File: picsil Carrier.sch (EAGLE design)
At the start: 43 parts, among them IC1 NAND, J1 STX-3120-3BM, J2 STX-3120-3BM, J3 STX-3120-3BM, J5 S2B-PH-SM4-TB(LF)(SN), J6 47346-1001, Q1 MMBT2222A, U1 MB85RC256VPF-G-JNERE2, U11 BORON, U2 TPL5010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

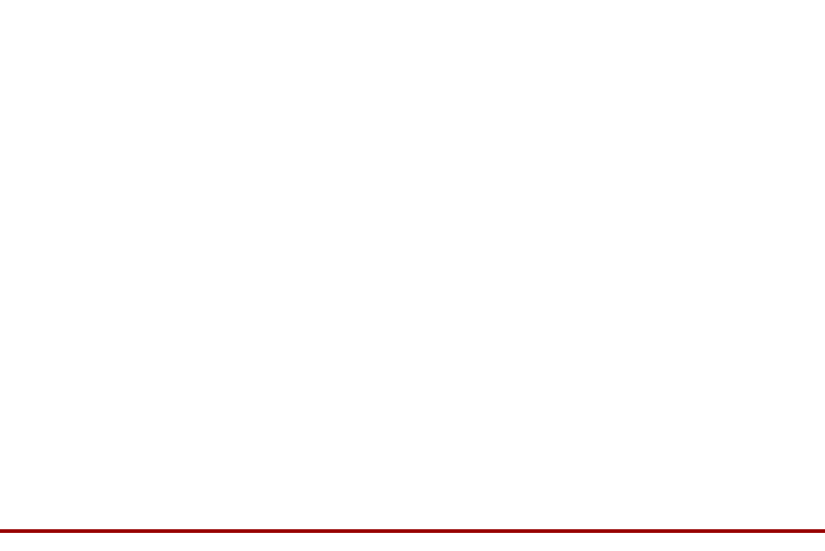
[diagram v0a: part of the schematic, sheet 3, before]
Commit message: mounting holes and fiducials
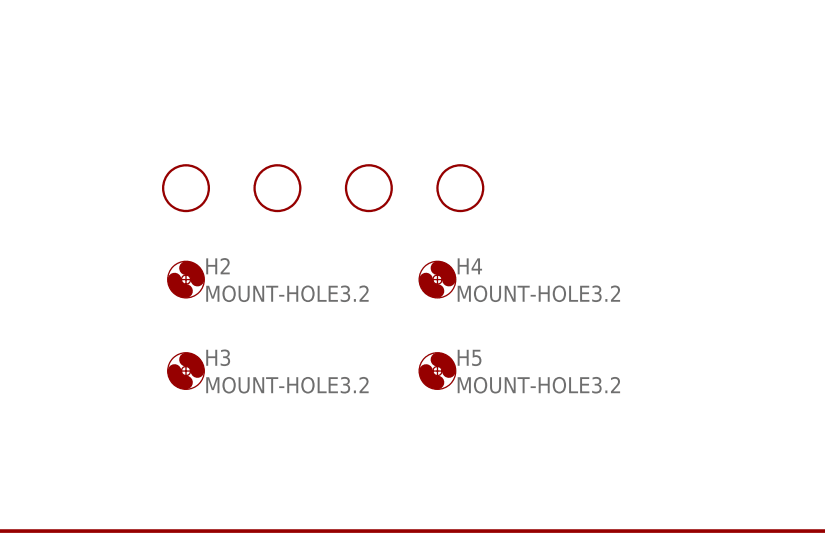
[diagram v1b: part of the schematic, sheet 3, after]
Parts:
- added H2, H3, H4, H5: MOUNT-HOLE3.2, holes:MOUNT-HOLE3.2
- added U$1, U$2, U$3, U$4: FIDUCIAL, adafruit:FIDUCIAL
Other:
- note added: "Fiducials and Holes"
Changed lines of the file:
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@@
 <setting verticaltext="up"/>
 </settings>
-<grid distance="0.1" unitdist="inch" unit="inch" style="lines" multiple="1" display="no" altdistance="0.01" altunitdist="inch" altunit="inch"/>
+<grid distance="0.1" unitdist="inch" unit="inch" style="lines" multiple="1" display="yes" altdistance="0.01" altunitdist="inch" altunit="inch"/>
 <layers>
 <layer number="1" name="Top" color="4" fill="1" visible="no" active="no"/>
@@
 <part name="J6" library="SamacSys_Parts" deviceset="47346-1001" device=""/>
 <part name="D4" library="SamacSys_Parts" deviceset="BYS12-90-M3_TR" device=""/>
+<part name="U$1" library="adafruit" library_urn="urn:adsk.eagle:library:420" deviceset="FIDUCIAL" device="" package3d_urn="urn:adsk.eagle:package:6240632/1"/>
+<part name="U$2" library="adafruit" library_urn="urn:adsk.eagle:library:420" deviceset="FIDUCIAL" device="" package3d_urn="urn:adsk.eagle:package:6240632/1"/>
+<part name="U$3" library="adafruit" library_urn="urn:adsk.eagle:library:420" deviceset="FIDUCIAL" device="" package3d_urn="urn:adsk.eagle:package:6240632/1"/>
+<part name="U$4" library="adafruit" library_urn="urn:adsk.eagle:library:420" deviceset="FIDUCIAL" device="" package3d_urn="urn:adsk.eagle:package:6240632/1"/>
+<part name="H2" library="holes" library_urn="urn:adsk.eagle:library:237" deviceset="MOUNT-HOLE" device="3.2" package3d_urn="urn:adsk.eagle:package:14275/1"/>
+<part name="H3" library="holes" library_urn="urn:adsk.eagle:library:237" deviceset="MOUNT-HOLE" device="3.2" package3d_urn="urn:adsk.eagle:package:14275/1"/>
+<part name="H4" library="holes" library_urn="urn:adsk.eagle:library:237" deviceset="MOUNT-HOLE" device="3.2" package3d_urn="urn:adsk.eagle:package:14275/1"/>
+<part name="H5" library="holes" library_urn="urn:adsk.eagle:library:237" deviceset="MOUNT-HOLE" device="3.2" package3d_urn="urn:adsk.eagle:package:14275/1"/>
 </parts>
 <sheets>
@@
 <text x="167.64" y="10.16" size="2.7432" layer="94">Reid Forrest</text>
 <text x="241.3" y="7.62" size="2.7432" layer="94">A</text>
+<text x="38.1" y="45.72" size="2.54" layer="127">Fiducials and Holes</text>
 </plain>
 <instances>
@@
 <attribute name="VALUE" x="82.55" y="104.14" size="1.778" layer="96" rot="R180" align="center-left"/>
 </instance>
+<instance part="U$1" gate="G$1" x="22.86" y="38.1" smashed="yes"/>
+<instance part="U$2" gate="G$1" x="33.02" y="38.1" smashed="yes"/>
+<instance part="U$3" gate="G$1" x="43.18" y="38.1" smashed="yes"/>
+<instance part="U$4" gate="G$1" x="53.34" y="38.1" smashed="yes"/>
+<instance part="H2" gate="G$1" x="22.86" y="27.94" smashed="yes">
+<attribute name="NAME" x="24.892" y="28.5242" size="1.778" layer="95"/>
+<attribute name="VALUE" x="24.892" y="25.4762" size="1.778" layer="96"/>
+</instance>
+<instance part="H3" gate="G$1" x="22.86" y="17.78" smashed="yes">
+<attribute name="NAME" x="24.892" y="18.3642" size="1.778" layer="95"/>
+<attribute name="VALUE" x="24.892" y="15.3162" size="1.778" layer="96"/>
+</instance>
+<instance part="H4" gate="G$1" x="50.8" y="27.94" smashed="yes">
+<attribute name="NAME" x="52.832" y="28.5242" size="1.778" layer="95"/>
+<attribute name="VALUE" x="52.832" y="25.4762" size="1.778" layer="96"/>
+</instance>
+<instance part="H5" gate="G$1" x="50.8" y="17.78" smashed="yes">
+<attribute name="NAME" x="52.832" y="18.3642" size="1.778" layer="95"/>
+<attribute name="VALUE" x="52.832" y="15.3162" size="1.778" layer="96"/>
+</instance>
 </instances>

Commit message: finalized Rev A
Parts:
- added FRAME4: FRAME-LETTER, SparkFun-Aesthetics:FRAME-LETTER
- FRAME1: _EXTERNAL_ 1 -> (none)
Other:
- note added: "Based in part on the Gen3 Carrier by Chip McClelland"
- moved on the sheet: J1, J2, J3
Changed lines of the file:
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@@
 <setting verticaltext="up"/>
 </settings>
-<grid distance="0.1" unitdist="inch" unit="inch" style="lines" multiple="1" display="yes" altdistance="0.01" altunitdist="inch" altunit="inch"/>
+<grid distance="0.1" unitdist="inch" unit="inch" style="lines" multiple="1" display="no" altdistance="0.01" altunitdist="inch" altunit="inch"/>
 <layers>
 <layer number="1" name="Top" color="4" fill="1" visible="no" active="no"/>
@@
 <layer number="110" name="fp0" color="7" fill="1" visible="yes" active="yes"/>
 <layer number="111" name="LPC17xx" color="7" fill="1" visible="yes" active="yes"/>
-<layer number="112" name="tSilk" color="7" fill="1" visible="yes" active="yes"/>
+<layer number="112" name="112bmp" color="1" fill="10" visible="yes" active="yes"/>
 <layer number="113" name="LOGO" color="7" fill="1" visible="yes" active="yes"/>
 <layer number="114" name="Badge_Outline" color="7" fill="1" visible="yes" active="yes"/>
@@
 <layer number="119" name="KAP_TEKEN" color="7" fill="1" visible="no" active="no"/>
 <layer number="120" name="KAP_MAAT1" color="7" fill="1" visible="no" active="no"/>
-<layer number="121" name="_tsilk" color="7" fill="1" visible="yes" active="yes"/>
+<layer number="121" name="121bmp" color="1" fill="10" visible="yes" active="yes"/>
 <layer number="122" name="_bsilk" color="7" fill="1" visible="yes" active="yes"/>
 <layer number="123" name="tTestmark" color="7" fill="1" visible="yes" active="yes"/>
@@
 <part name="SUPPLY3" library="supply2" library_urn="urn:adsk.eagle:library:372" deviceset="GND" device=""/>
 <part name="SUPPLY1" library="supply2" library_urn="urn:adsk.eagle:library:372" deviceset="GND" device=""/>
-<part name="FRAME1" library="SparkFun-Aesthetics" library_urn="urn:adsk.eagle:library:507" deviceset="FRAME-LETTER" device="" package3d_urn="urn:adsk.eagle:package:37121/1">
-<attribute name="_EXTERNAL_" value="1"/>
-</part>
 <part name="FRAME2" library="SparkFun-Aesthetics" library_urn="urn:adsk.eagle:library:507" deviceset="FRAME-LETTER" device="" package3d_urn="urn:adsk.eagle:package:37121/1"/>
 <part name="FRAME3" library="SparkFun-Aesthetics" library_urn="urn:adsk.eagle:library:507" deviceset="FRAME-LETTER" device="" package3d_urn="urn:adsk.eagle:package:37121/1"/>
@@
 <part name="H4" library="holes" library_urn="urn:adsk.eagle:library:237" deviceset="MOUNT-HOLE" device="3.2" package3d_urn="urn:adsk.eagle:package:14275/1"/>
 <part name="H5" library="holes" library_urn="urn:adsk.eagle:library:237" deviceset="MOUNT-HOLE" device="3.2" package3d_urn="urn:adsk.eagle:package:14275/1"/>
+<part name="FRAME1" library="SparkFun-Aesthetics" library_urn="urn:adsk.eagle:library:507" deviceset="FRAME-LETTER" device="" package3d_urn="urn:adsk.eagle:package:37121/1"/>
+<part name="FRAME4" library="SparkFun-Aesthetics" library_urn="urn:adsk.eagle:library:507" deviceset="FRAME-LETTER" device="" package3d_urn="urn:adsk.eagle:package:37121/1"/>
 </parts>
 <sheets>
@@
 <text x="167.64" y="10.16" size="2.7432" layer="94">Reid Forrest</text>
 <text x="241.3" y="7.62" size="2.7432" layer="94">A</text>
+<text x="78.74" y="2.54" size="1.778" layer="97">Based in part on the Gen3 Carrier by Chip McClelland</text>
 </plain>
 <instances>
@@
 <attribute name="VALUE" x="76.835" y="111.125" size="1.778" layer="96"/>
 </instance>
-<instance part="J1" gate="G$1" x="12.7" y="25.4" smashed="yes">
-<attribute name="NAME" x="34.29" y="33.02" size="1.778" layer="95" align="center-left"/>
-<attribute name="VALUE" x="34.29" y="30.48" size="1.778" layer="96" align="center-left"/>
-</instance>
-<instance part="J2" gate="G$1" x="58.42" y="25.4" smashed="yes">
-<attribute name="NAME" x="80.01" y="33.02" size="1.778" layer="95" align="center-left"/>
-<attribute name="VALUE" x="80.01" y="30.48" size="1.778" layer="96" align="center-left"/>
-</instance>
-<instance part="J3" gate="G$1" x="104.14" y="25.4" smashed="yes">
-<attribute name="NAME" x="125.73" y="33.02" size="1.778" layer="95" align="center-left"/>
-<attribute name="VALUE" x="125.73" y="30.48" size="1.778" layer="96" align="center-left"/>
-</instance>
-<instance part="SUPPLY6" gate="GND" x="99.06" y="10.16" smashed="yes">
-<attribute name="VALUE" x="97.155" y="6.985" size="1.778" layer="96"/>
-</instance>
-<instance part="SUPPLY3" gate="GND" x="53.34" y="10.16" smashed="yes">
-<attribute name="VALUE" x="51.435" y="6.985" size="1.778" layer="96"/>
-</instance>
-<instance part="SUPPLY1" gate="GND" x="5.08" y="10.16" smashed="yes">
-<attribute name="VALUE" x="3.175" y="6.985" size="1.778" layer="96"/>
+<instance part="J1" gate="G$1" x="12.7" y="30.48" smashed="yes">
+<attribute name="NAME" x="34.29" y="38.1" size="1.778" layer="95" align="center-left"/>
+<attribute name="VALUE" x="34.29" y="35.56" size="1.778" layer="96" align="center-left"/>
+</instance>
+<instance part="J2" gate="G$1" x="58.42" y="30.48" smashed="yes">
+<attribute name="NAME" x="80.01" y="38.1" size="1.778" layer="95" align="center-left"/>
+<attribute name="VALUE" x="80.01" y="35.56" size="1.778" layer="96" align="center-left"/>
+</instance>
+<instance part="J3" gate="G$1" x="104.14" y="30.48" smashed="yes">
+<attribute name="NAME" x="125.73" y="38.1" size="1.778" layer="95" align="center-left"/>
+<attribute name="VALUE" x="125.73" y="35.56" size="1.778" layer="96" align="center-left"/>
+</instance>
+<instance part="SUPPLY6" gate="GND" x="99.06" y="15.24" smashed="yes">
+<attribute name="VALUE" x="97.155" y="12.065" size="1.778" layer="96"/>
+</instance>
+<instance part="SUPPLY3" gate="GND" x="53.34" y="15.24" smashed="yes">
+<attribute name="VALUE" x="51.435" y="12.065" size="1.778" layer="96"/>
+</instance>
+<instance part="SUPPLY1" gate="GND" x="5.08" y="15.24" smashed="yes">
+<attribute name="VALUE" x="3.175" y="12.065" size="1.778" layer="96"/>
 </instance>
 <instance part="FRAME1" gate="G$1" x="0" y="0" smashed="yes"/>
-<instance part="FRAME1" gate="V" x="147.32" y="0" smashed="yes">
+<instance part="FRAME4" gate="V" x="147.32" y="0" smashed="yes">
 <attribute name="LAST_DATE_TIME" x="160.02" y="1.27" size="2.54" layer="94" font="vector"/>
 <attribute name="SHEET" x="233.68" y="1.27" size="2.54" layer="94" font="vector"/>
 <attribute name="DRAWING_NAME" x="162.814" y="17.78" size="2.7432" layer="94" font="vector"/>
-<attribute name="_EXTERNAL_" x="147.32" y="0" size="1.778" layer="96" display="off"/>
 </instance>
 </instances>
@@
 <pinref part="SUPPLY1" gate="GND" pin="GND"/>
 <pinref part="J1" gate="G$1" pin="1"/>
-<wire x1="5.08" y1="12.7" x2="5.08" y2="25.4" width="0.1524" layer="91"/>
-<wire x1="5.08" y1="25.4" x2="12.7" y2="25.4" width="0.1524" layer="91"/>
+<wire x1="5.08" y1="17.78" x2="5.08" y2="30.48" width="0.1524" layer="91"/>
+<wire x1="5.08" y1="30.48" x2="12.7" y2="30.48" width="0.1524" layer="91"/>
 </segment>
 <segment>
 <pinref part="SUPPLY3" gate="GND" pin="GND"/>
 <pinref part="J2" gate="G$1" pin="1"/>
-<wire x1="53.34" y1="12.7" x2="53.34" y2="25.4" width="0.1524" layer="91"/>
-<wire x1="53.34" y1="25.4" x2="58.42" y2="25.4" width="0.1524" layer="91"/>
+<wire x1="53.34" y1="17.78" x2="53.34" y2="30.48" width="0.1524" layer="91"/>
+<wire x1="53.34" y1="30.48" x2="58.42" y2="30.48" width="0.1524" layer="91"/>
 </segment>
 <segment>
 <pinref part="SUPPLY6" gate="GND" pin="GND"/>
 <pinref part="J3" gate="G$1" pin="1"/>
-<wire x1="99.06" y1="12.7" x2="99.06" y2="25.4" width="0.1524" layer="91"/>
-<wire x1="99.06" y1="25.4" x2="104.14" y2="25.4" width="0.1524" layer="91"/>
+<wire x1="99.06" y1="17.78" x2="99.06" y2="30.48" width="0.1524" layer="91"/>
+<wire x1="99.06" y1="30.48" x2="104.14" y2="30.48" width="0.1524" layer="91"/>
 </segment>
 </net>
@@
 <segment>
 <pinref part="J3" gate="G$1" pin="5"/>
-<wire x1="104.14" y1="20.32" x2="104.14" y2="15.24" width="0.1524" layer="91"/>
-<label x="104.14" y="15.24" size="1.778" layer="95"/>
+<wire x1="104.14" y1="25.4" x2="104.14" y2="20.32" width="0.1524" layer="91"/>
+<label x="104.14" y="20.32" size="1.778" layer="95"/>
 </segment>
 </net>
@@
 <segment>
 <pinref part="J2" gate="G$1" pin="5"/>
-<wire x1="58.42" y1="20.32" x2="58.42" y2="15.24" width="0.1524" layer="91"/>
-<label x="58.42" y="15.24" size="1.778" layer="95"/>
+<wire x1="58.42" y1="25.4" x2="58.42" y2="20.32" width="0.1524" layer="91"/>
+<label x="58.42" y="20.32" size="1.778" layer="95"/>
 </segment>
 </net>
@@
 <segment>
 <pinref part="J1" gate="G$1" pin="5"/>
-<wire x1="12.7" y1="20.32" x2="12.7" y2="15.24" width="0.1524" layer="91"/>
-<label x="12.7" y="15.24" size="1.778" layer="95"/>
+<wire x1="12.7" y1="25.4" x2="12.7" y2="20.32" width="0.1524" layer="91"/>
+<label x="12.7" y="20.32" size="1.778" layer="95"/>
 </segment>
 </net>
@@
 <segment>
 <pinref part="J1" gate="G$1" pin="MH2"/>
-<wire x1="38.1" y1="25.4" x2="40.64" y2="25.4" width="0.1524" layer="91"/>
-<label x="40.64" y="25.4" size="1.778" layer="95"/>
+<wire x1="38.1" y1="30.48" x2="40.64" y2="30.48" width="0.1524" layer="91"/>
+<label x="40.64" y="30.48" size="1.778" layer="95"/>
 </segment>
 <segment>
 <pinref part="J2" gate="G$1" pin="MH2"/>
-<wire x1="83.82" y1="25.4" x2="86.36" y2="25.4" width="0.1524" layer="91"/>
-<label x="86.36" y="25.4" size="1.778" layer="95"/>
+<wire x1="83.82" y1="30.48" x2="86.36" y2="30.48" width="0.1524" layer="91"/>
+<label x="86.36" y="30.48" size="1.778" layer="95"/>
 </segment>
 <segment>
 <pinref part="J3" gate="G$1" pin="MH2"/>
-<wire x1="129.54" y1="25.4" x2="132.08" y2="25.4" width="0.1524" layer="91"/>
-<label x="132.08" y="25.4" size="1.778" layer="95"/>
-</segment>
-</net>
+<wire x1="129.54" y1="30.48" x2="132.08" y2="30.48" width="0.1524" layer="91"/>
+<label x="132.08" y="30.48" size="1.778" layer="95"/>
+</segment>
+</net>
